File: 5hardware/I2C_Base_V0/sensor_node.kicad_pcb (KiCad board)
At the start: 2 copper layers, 57 parts, among them J1 USB_C_Receptacle_USB2.0, J2 PJ-320D-A, J3 Conn_02x06_Top_Bottom, J4 Conn_01x19_Socket, J5 Conn_01x19_Socket, J6 Conn_01x06_Socket, P1 S3B-PH-SM4-TB, P2 S4B-PH-SM4-TB, P3 S3B-PH-SM4-TB, Q2 Si2371EDS, Q3 Si2371EDS, SW2 SW_Push, SW3 SW_Push, U1 MCP1700x-330xxTO, U10 ESP-12F, U12 APDS-9960, U14 DS3231M, U3 CR2450, U4 CH32V003F4P6, U5 SHT31-DIS, U6 DS1307Z+, U7 XC6206PxxxMR, U8 TPL5110, U9 BH1750FVI-TR, Y1 Crystal

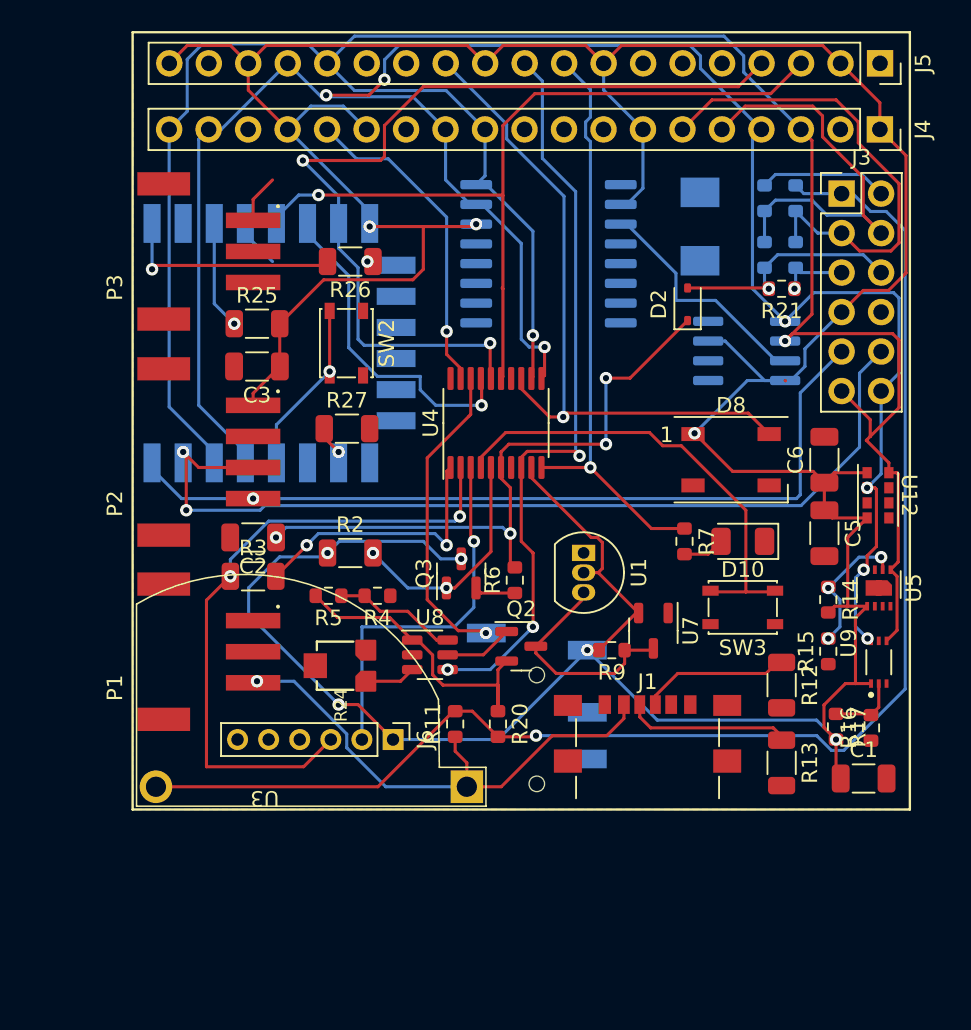
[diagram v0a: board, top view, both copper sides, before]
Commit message: update schematic.
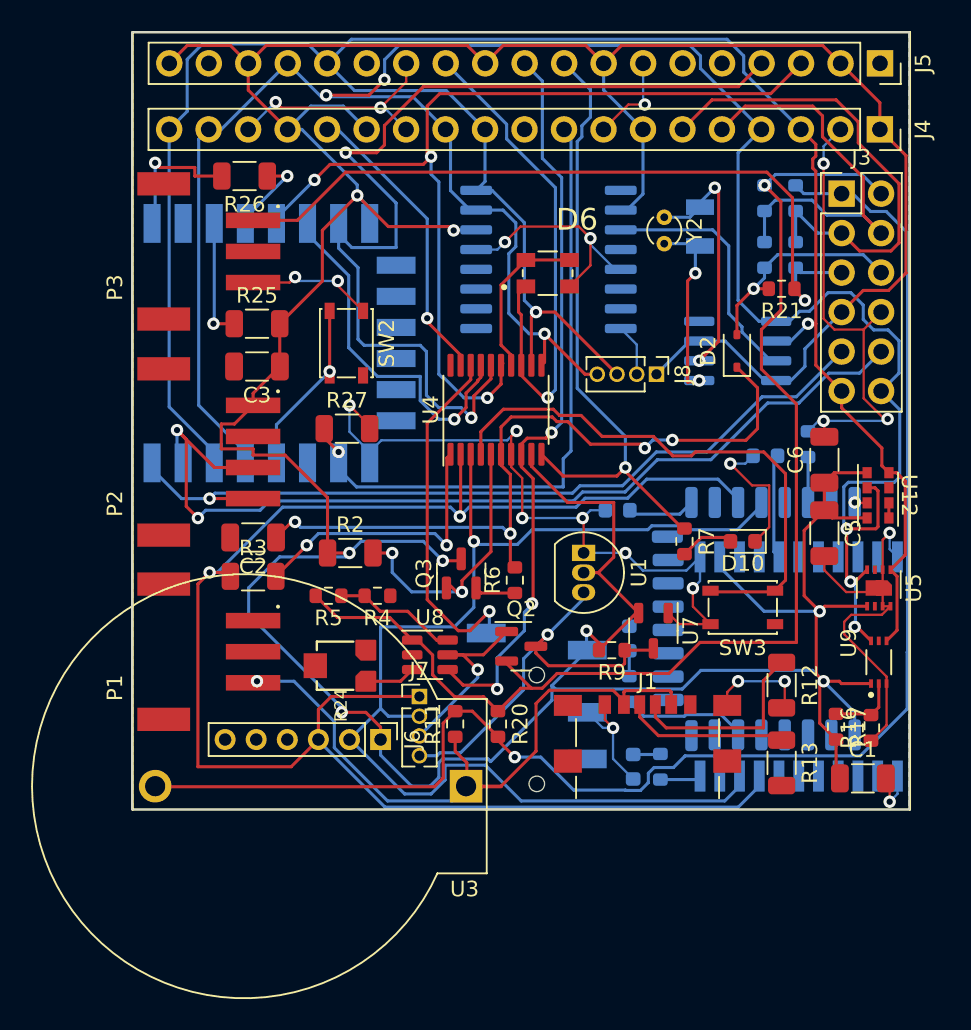
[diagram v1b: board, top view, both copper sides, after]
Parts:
- removed D8: WS2812B, LED_SMD:LED_WS2812B_PLCC4_5.0x5.0mm_P3.2mm
- removed R14, R15: R, Resistor_SMD:R_0603_1608Metric
- added D1: LED, LED_SMD:LED_0603_1608Metric, B.Cu at (132.0, 114.2)
- added D3: LED, LED_SMD:LED_0603_1608Metric, B.Cu at (131.2, 106.0)
- added D4: LED, LED_SMD:LED_0603_1608Metric, B.Cu at (140.8, 102.5)
- added D5: LED, LED_SMD:LED_0603_1608Metric, B.Cu at (132.2, 122.5)
- added D6: LL-R3528RGBC-008-B, R3528RGB:LED_LL-R3528RGBC-008-B, F.Cu at (126.8, 90.8)
- added J7: Conn_01x04_Pin, Connector_PinHeader_1.27mm:PinHeader_1x04_P1.27mm_Vertical, F.Cu at (118.5, 118.0)
- added J8: Conn_01x04_Pin, Connector_PinHeader_1.27mm:PinHeader_1x04_P1.27mm_Vertical, F.Cu at (133.8, 97.2)
- added R1: R, Resistor_SMD:R_0603_1608Metric, B.Cu at (143.5, 101.8)
- added R10: R, Resistor_SMD:R_0603_1608Metric, B.Cu at (134.0, 122.5)
- added R8: R, Resistor_SMD:R_0603_1608Metric, B.Cu at (132.0, 117.5)
- added U11: ~, A_SensorNode:JDY-Base, B.Cu at (134.5, 105.5)
- added U2: ~, A_SensorNode:E104-BT07, B.Cu at (150.2, 124.3)
- added Y2: Crystal, Crystal:Crystal_Round_D1.5mm_Vertical, F.Cu at (134.2, 87.2)
- D10: footprint LED_SMD:LED_1206_3216Metric -> LED_SMD:LED_0603_1608Metric
- U3: footprint A_SensorNode:CR2450 -> Battery:BatteryHolder_ComfortableElectronic_CH273-2450_1x2450
- Y1: footprint Crystal:Crystal_SMD_0603-2Pin_6.0x3.5mm -> Crystal:Crystal_SMD_3215-2Pin_3.2x1.5mm
- moved U3 14.5 mm to (121.5, 123.8)
- moved R26 8.75 mm to (107.2, 84.5)
- moved D2 4.37 mm to (138.9, 95.8)
- moved U4 0.85 mm to (123.4, 99.5)
- moved J6 0.80 mm to (116.0, 120.8)
- moved U6 0.58 mm to (139.0, 95.8)
- moved U14 0.36 mm to (126.8, 89.9)
- moved C1 0.05 mm to (147.0, 123.2)
- turned Y1 to 90 degrees
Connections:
- net Net-(Q2-D) renamed Vo
- net Net-(Q2-G) renamed DRV
- U4 pad 14: unconnected-(U4-PC4-Pad14) -> Net-(U4-PC4)
- U5 pad 2: Net-(U5-ADDR) -> GND
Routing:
- net GND: track 0.17 -> 176.8 mm, vias 0 -> 23
- net RX: track 41.8 -> 104.7 mm
- net TX: track 24.1 -> 77.1 mm
- net Bat-Vo: track 28.3 -> 78.6 mm, vias 0 -> 1
- net Solar_Vi: track 7.59 -> 49.0 mm
- net D15: track 1.88 -> 41.3 mm
- net VCC: track 266.3 -> 294.5 mm
- net Net-(U6-X2): track 0.00 -> 16.0 mm, vias 0 -> 2
- net SDA (4): track 139.6 -> 154.8 mm, vias 7 -> 6
- net Vo: track 14.5 -> 27.1 mm, vias 0 -> 1
- net Net-(U6-X1): track 0.00 -> 12.2 mm, vias 0 -> 2
- net Net-(J5-Pin_12): track 43.9 -> 33.1 mm
- net Net-(U4-PC4): track 0.00 -> 10.5 mm
- net +5V: track 33.5 -> 43.8 mm
- net Net-(U5-ADDR): track 9.02 -> 0.00 mm, vias 3 -> 0
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- added copper zone on B.Cu, net GND
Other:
- board outline added: 50 x 50 mm
- board text added: "MOSI"
- board text added: "SCK"
- board text removed: "0D0"
- board text removed: "1"
- board text removed: "12"
- board text removed: "13"
- board text removed: "14"
- board text removed: "15"
- board text removed: "16"
- board text removed: "18"
- board text removed: "19"
- board text removed: "21"
- board text removed: "22"
- board text removed: "23"
- board text removed: "3"
- board text removed: "32"
- board text removed: "33"
- board text removed: "34"
- board text removed: "35"
- board text removed: "36"
- board text removed: "39"
- board text removed: "4"
- board text removed: "5"
- board text removed: "5V"
- board text removed: "ADC"
- board text removed: "D1"
- board text removed: "D2"
- board text removed: "D3"
- board text removed: "D4"
- board text removed: "D5"
- board text removed: "IO0"
- board text removed: "LK"
- board text removed: "OD0"
- board text removed: "OD1"
- board text removed: "OD2"
- board text removed: "OD4"
- board text removed: "OD5"
- board text removed: "PA1"
- board text removed: "PA2"
- board text removed: "PC0"
- board text removed: "PC4"
- board text removed: "PC5"
- board text removed: "PC6"
- board text removed: "PC7"
- board text removed: "PD0"
- board text removed: "RST"

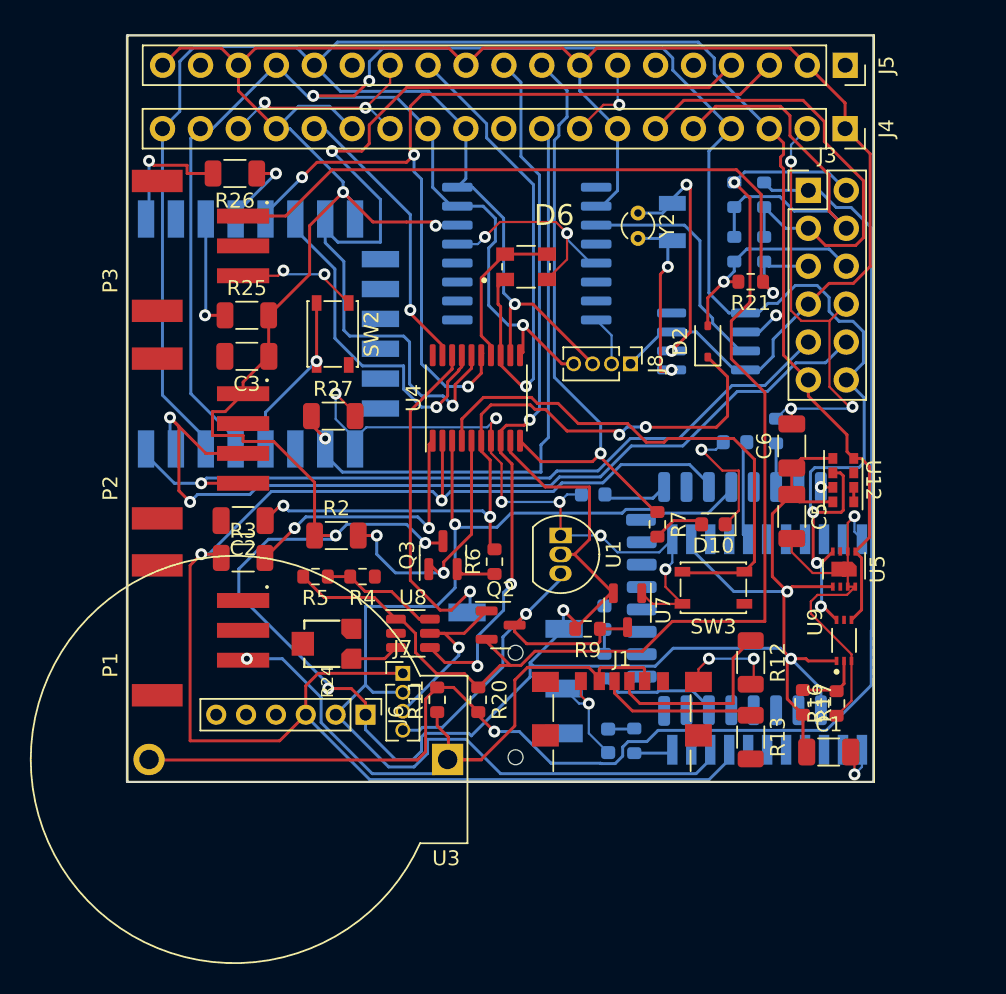
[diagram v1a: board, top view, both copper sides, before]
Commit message: update schematic.
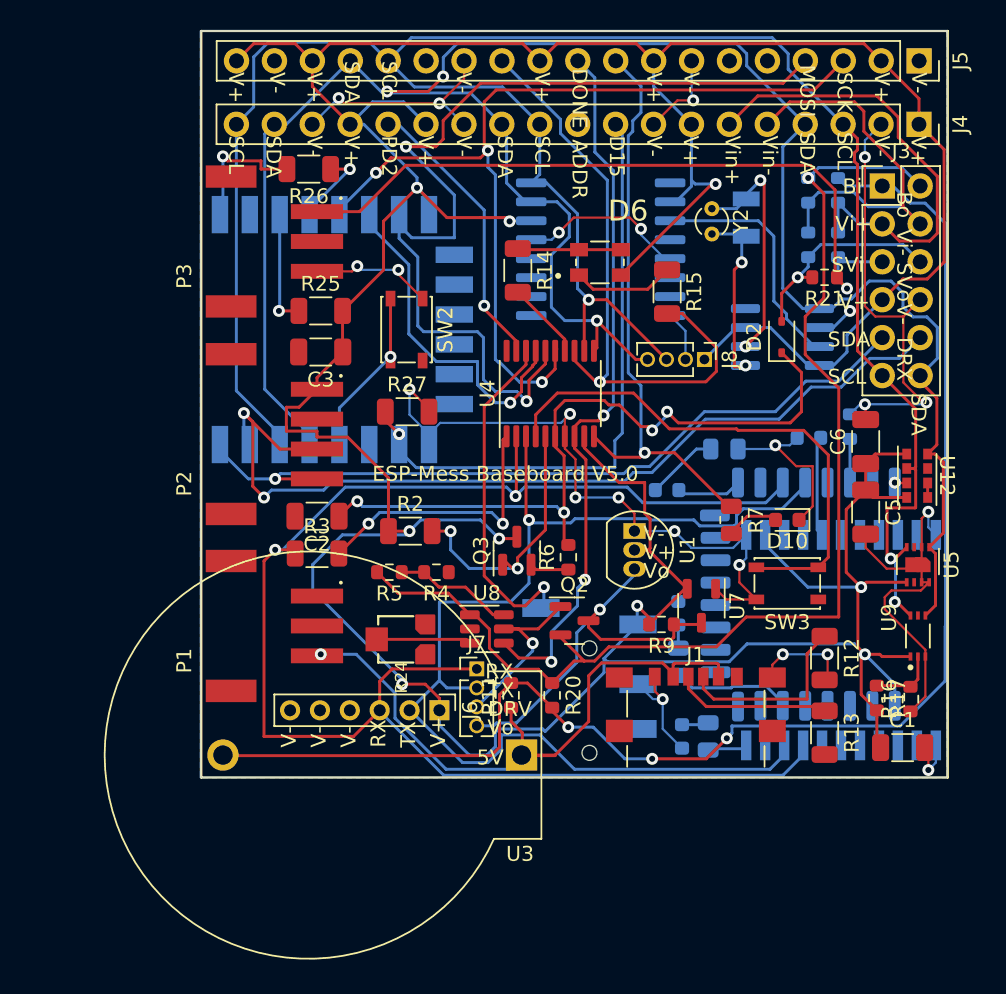
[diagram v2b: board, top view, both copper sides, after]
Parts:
- added R14: R, Resistor_SMD:R_1206_3216Metric, F.Cu at (126.2, 91.0)
- added R15: R, Resistor_SMD:R_1206_3216Metric, F.Cu at (136.2, 92.4)
- added R28: R, Resistor_SMD:R_0805_2012Metric, B.Cu at (140.0, 103.0)
- R10, R7, R8: footprint Resistor_SMD:R_0603_1608Metric -> Resistor_SMD:R_0805_2012Metric
- moved C1 4.96 mm to (152.0, 123.0)
- moved C2 4.96 mm to (112.8, 107.5)
- moved C3 4.96 mm to (113.0, 96.5)
- moved C5 4.96 mm to (149.5, 107.2)
- moved C6 4.96 mm to (149.5, 102.5)
- moved D1 4.96 mm to (136.9, 114.0)
- moved D10 4.96 mm to (144.2, 107.7)
- moved D2 4.96 mm to (143.9, 95.5)
- moved D3 4.96 mm to (136.2, 105.7)
- moved D4 4.96 mm to (145.7, 102.2)
- moved D5 4.96 mm to (137.2, 122.2)
- moved D6 4.96 mm to (131.7, 90.5)
- moved J1 4.96 mm to (138.1, 121.2)
- moved J2 4.96 mm to (131.0, 119.4)
- moved J3 4.96 mm to (150.6, 85.3)
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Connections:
- D3 pad 1: GND -> Net-(D3-K)
- D6 pad 1: Net-(J5-Pin_12) -> Net-(D6-Pad1)
- D6 pad 2: GND -> VCC
- D6 pad 3: Net-(U4-PC4) -> Net-(D6-Pad3)
- D6 pad 4: Net-(U4-PC4) -> Net-(D6-Pad3)
- R24 pad 1: Net-(U8-DELAY/M_DRV) -> unconnected-(R24-Pad1)
- R24 pad 2: unconnected-(R24-Pad2) -> Net-(U8-DELAY/M_DRV)
- U12 pad 1: SCL (5) -> SDA (4)
- U12 pad 7: SDA (4) -> SCL (5)
- U5 pad 1: SCL (5) -> SDA (4)
- U5 pad 4: SDA (4) -> SCL (5)
- U9 pad 4: SCL (5) -> SDA (4)
- U9 pad 6: SDA (4) -> SCL (5)
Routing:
- net VCC: track 294.5 -> 303.6 mm, vias 8 -> 9
- net Net-(J5-Pin_12): track 33.1 -> 41.5 mm
- net SDA (4): track 154.8 -> 146.8 mm, vias 6 -> 3
- net Net-(D6-Pad3): track 0.00 -> 6.93 mm
- net Net-(D6-Pad1): track 0.00 -> 6.43 mm
- net Net-(U4-PC4): track 10.5 -> 5.23 mm
- net Net-(D3-K): track 0.00 -> 4.85 mm
- net GND: track 176.8 -> 173.5 mm
- net Net-(U8-DELAY/M_DRV): track 3.30 -> 6.34 mm
- net SCL (5): track 147.5 -> 150.3 mm, vias 2 -> 4
- net Net-(J5-Pin_9): track 40.1 -> 39.2 mm
- net Net-(D2-K): track 47.8 -> 48.6 mm
- net TX: track 77.1 -> 77.6 mm
- net Bat-Vi: track 96.3 -> 96.2 mm, vias 1 -> 3
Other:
- board text added: "5V"
- board text added: "ADDR"
- board text added: "Bi"
- board text added: "Bo"
- board text added: "D15"
- board text added: "DONE"
- board text added: "DRV"
- board text added: "DRX"
- board text added: "DTX"
- board text added: "ESP-Mess Baseboard V5.0"
- board text added: "PD2"
- board text added: "RX"
- board text added: "SCL"
- board text added: "SDA"
- board text added: "SVi"
- board text added: "SVo"
- board text added: "TX"
- board text added: "Vi+"
- board text added: "Vi-"
- board text added: "Vin+"
- board text added: "Vin-"
- board text added: "Vo"
- board text removed: "ESP-Mess Baseboard V3.0"

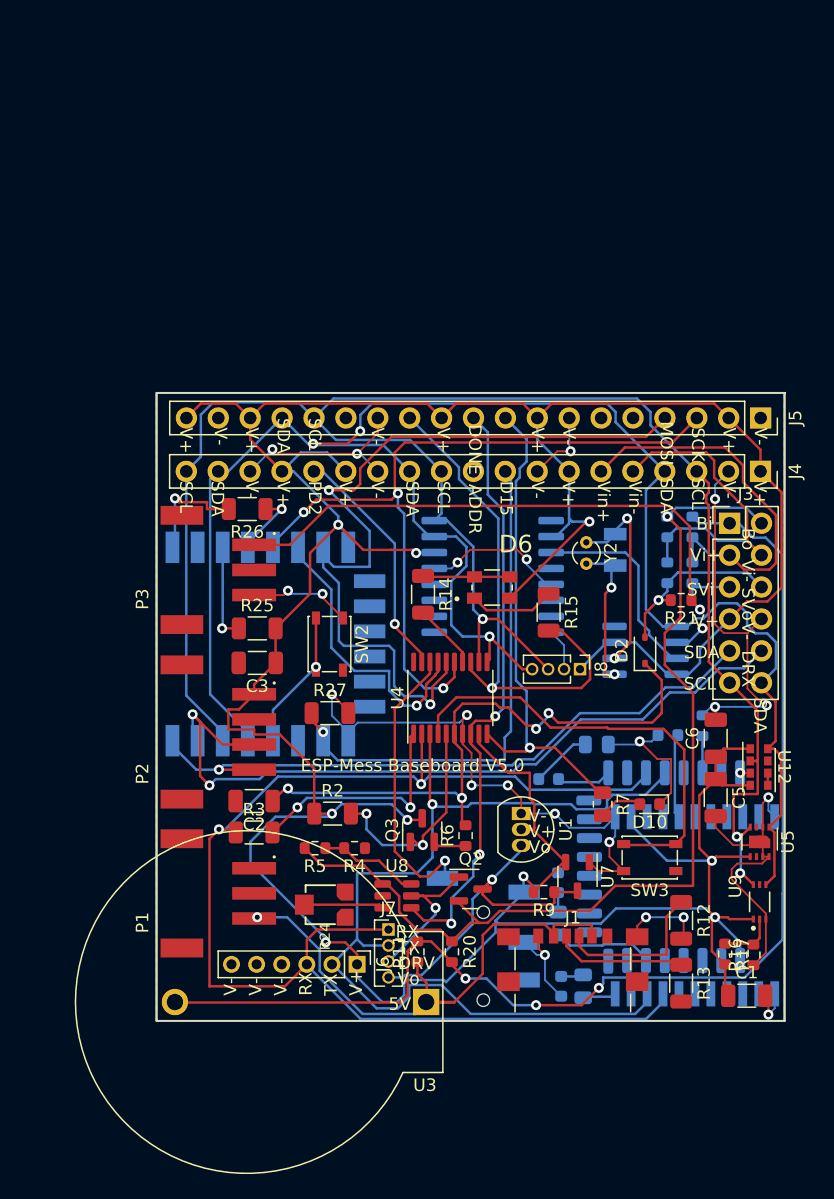
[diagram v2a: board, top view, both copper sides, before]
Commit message: update schematic.
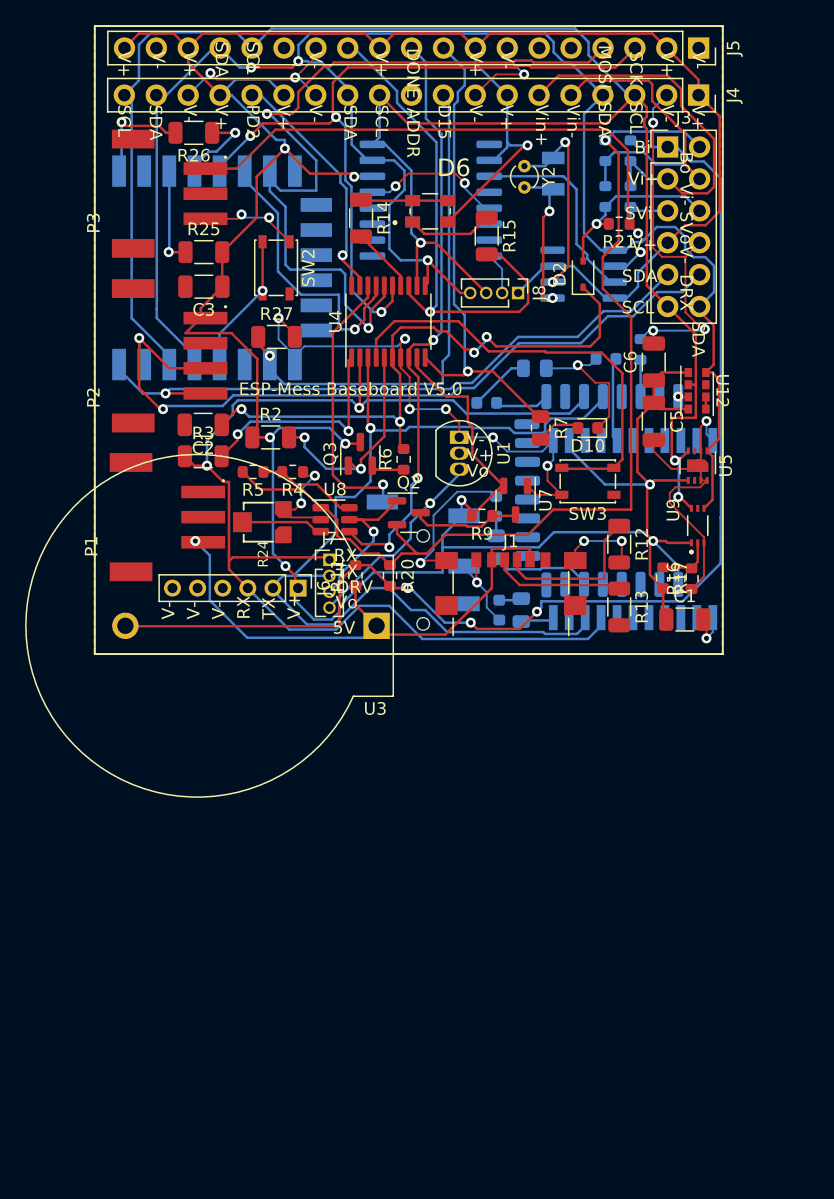
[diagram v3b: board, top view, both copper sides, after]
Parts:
- moved R24 30.9 mm to (113.5, 85.2)
- moved C1 30.4 mm to (147.0, 93.0)
- moved R15 30.4 mm to (131.3, 62.5)
- moved R18 30.4 mm to (142.7, 55.7)
- moved R19 30.4 mm to (140.7, 55.7)
- moved R22 30.4 mm to (142.7, 59.3)
- moved R23 30.4 mm to (140.7, 59.3)
- moved R28 30.4 mm to (135.1, 73.0)
- moved Y2 30.4 mm to (134.3, 56.9)
- moved C5 30.4 mm to (144.6, 77.2)
- moved C6 30.4 mm to (144.6, 72.5)
- moved D1 30.4 mm to (132.0, 84.0)
- moved D10 30.4 mm to (139.3, 77.8)
- moved D2 30.4 mm to (138.9, 65.5)
- moved D3 30.4 mm to (131.3, 75.8)
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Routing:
- net GND: track 173.5 -> 194.8 mm, vias 23 -> 26
- net VCC: track 303.6 -> 291.2 mm
- net RX: track 104.3 -> 93.6 mm
- net SCL (5): track 150.3 -> 160.1 mm
- net SDA (4): track 146.8 -> 142.8 mm
- net SCK: track 61.8 -> 60.2 mm
- net +5V: track 43.8 -> 42.2 mm
- net TX: track 77.6 -> 76.2 mm
- net D16: track 6.16 -> 7.29 mm
- net Vo: track 27.1 -> 26.0 mm
- net Bat-Vi: track 96.2 -> 95.1 mm
- net D-: track 18.7 -> 17.8 mm
- net D3_RX: track 62.1 -> 61.2 mm
- net SWIO: track 23.1 -> 22.2 mm
- net D1_TX: track 53.0 -> 52.3 mm
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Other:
- board outline removed
